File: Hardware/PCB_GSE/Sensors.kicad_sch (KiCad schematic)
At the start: 19 parts, among them J18 Screw_Terminal_01x04, J19 Screw_Terminal_01x04, U4 INA125UA/2K5, U6 INA125UA/2K5, U9 MAX6612MXK

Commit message: refactor: merge emile + main branches
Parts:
- renumbered C45 to C48, C44 to C49, C49 to C50, C48 to C51, C46 to C52, C47 to C53, J18 to J7, J19 to J8, R55 to R33, R53 to R34, R56 to R35, R54 to R36, R58 to R37, R57 to R38, U4 to U10, U9 to U11, U6 to U9

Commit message: fix: labels
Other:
- moved on the sheet: C48, C51, D6, J7, R33, R35, R38, U9

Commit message: wip : Reduce BOM and fill all datasheet, digikey and MPN
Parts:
- C48, C49, C50, C51, C53: footprint Capacitor_SMD:C_0805_2012Metric -> Capacitor_SMD:C_0603_1608Metric; DigiKey_Part_Number (none) -> 399-C0603C104K3RACTUCT-ND; Manufacturer_Part_Number (none) -> C0603C104K3RACTU
- C52: footprint Capacitor_SMD:C_0603_1608Metric -> Capacitor_SMD:C_0805_2012Metric; DigiKey_Part_Number (none) -> 1276-2434-1-ND; Manufacturer_Part_Number (none) -> CL21B103KAANNNC
- D5, D6: DigiKey_Part_Number (none) -> 4878-BAT54SCT-ND; Manufacturer_Part_Number (none) -> BAT54S
- J7, J8: DigiKey_Part_Number (none) -> ED10563-ND; Manufacturer_Part_Number (none) -> OSTVN04A150
- R33, R34: DigiKey_Part_Number (none) -> 311-10.0KHRCT-ND; Manufacturer_Part_Number (none) -> RC0603FR-0710KL
- R35: DigiKey_Part_Number (none) -> YAG3707CT-ND; Manufacturer_Part_Number (none) -> AC0805FR-07200RL
- R36: DigiKey_Part_Number (none) -> 311-1.00KCRCT-ND; Manufacturer_Part_Number (none) -> RC0805FR-071KL
- R37, R38: DigiKey_Part_Number (none) -> P1.5KDBCT-ND; Manufacturer_Part_Number (none) -> ERA-3AEB152V
- U10, U9: DigiKey_Part_Number (none) -> 296-50343-1-ND; DigiKey_Part_Number  296-50343-1-ND -> (none)

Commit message: wip: begining layout
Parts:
- renumbered R33 to R36, R34 to R37, R35 to R38, R36 to R39, R37 to R40, R38 to R41

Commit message: wip : subsystems layout
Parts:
- renumbered C48 to C57, C49 to C58, C50 to C59, C51 to C60, C52 to C61, C53 to C62, D5 to D4, D6 to D5, R36 to R44, R37 to R45, R38 to R46, R39 to R47, R40 to R48, R41 to R49

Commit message: wip : Done routing
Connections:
- net +3.3VA is gone; now on net +3V3: D4.2 (K), D5.2 (K)
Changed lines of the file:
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@@
-	)
-	(symbol
-		(lib_id "power:+3.3VA")
-		(at 127 130.81 0)
-		(unit 1)
-		(exclude_from_sim no)
-		(in_bom yes)
-		(on_board yes)
-		(dnp no)
-		(property "Reference" "#PWR0222"
-			(at 127 134.62 0)
-			(effects
-				(font
-					(size 1 1)
-				)
-				(hide yes)
-			)
-		)
-		(property "Value" "+3.3VA"
-			(at 127 127 0)
-			(effects
-				(font
-					(size 1 1)
-				)
-			)
-		)
-		(property "Footprint" ""
-			(at 127 130.81 0)
-			(effects
-				(font
-					(size 1 1)
-				)
-				(hide yes)
-			)
-		)
-		(property "Datasheet" ""
-			(at 127 130.81 0)
-			(effects
-				(font
-					(size 1 1)
-				)
-				(hide yes)
-			)
-		)
-		(property "Description" ""
-			(at 127 130.81 0)
-			(effects
-				(font
-					(size 1.27 1.27)
-				)
-			)
-		)
-		(pin "1"
-		)
-		(instances
-			(project "PCB_GSE"
-				(path "/a63f9ed4-21e4-42d0-8bfc-f96143f84d4d/03aa44f0-76dc-422b-9f36-66afc2e68b3b"
-					(reference "#PWR0222")
-					(unit 1)
-				)
-			)
-		)
 	)
 	(symbol
@@
 	)
 	(symbol
+		(lib_id "power:+3V3")
+		(at 127 130.81 0)
+		(unit 1)
+		(exclude_from_sim no)
+		(in_bom yes)
+		(on_board yes)
+		(dnp no)
+		(property "Reference" "#PWR03"
+			(at 127 134.62 0)
+			(effects
+				(font
+					(size 1.27 1.27)
+				)
+				(hide yes)
+			)
+		)
+		(property "Value" "+3V3"
+			(at 127 127 0)
+			(effects
+				(font
+					(size 1.27 1.27)
+				)
+			)
+		)
+		(property "Footprint" ""
+			(at 127 130.81 0)
+			(effects
+				(font
+					(size 1.27 1.27)
+				)
+				(hide yes)
+			)
+		)
+		(property "Datasheet" ""
+			(at 127 130.81 0)
+			(effects
+				(font
+					(size 1.27 1.27)
+				)
+				(hide yes)
+			)
+		)
+		(property "Description" "Power symbol creates a global label with name \"+3V3\""
+			(at 127 130.81 0)
+			(effects
+				(font
+					(size 1.27 1.27)
+				)
+				(hide yes)
+			)
+		)
+		(pin "1"
+		)
+		(instances
+			(project "PCB_GSE"
+				(path "/a63f9ed4-21e4-42d0-8bfc-f96143f84d4d/03aa44f0-76dc-422b-9f36-66afc2e68b3b"
+					(reference "#PWR03")
+					(unit 1)
+				)
+			)
+		)
+	)
+	(symbol
 		(lib_id "Device:C")
 		(at 257.81 44.45 0)
@@
 	)
 	(symbol
+		(lib_id "power:+3V3")
+		(at 127 57.15 0)
+		(unit 1)
+		(exclude_from_sim no)
+		(in_bom yes)
+		(on_board yes)
+		(dnp no)
+		(property "Reference" "#PWR04"
+			(at 127 60.96 0)
+			(effects
+				(font
+					(size 1.27 1.27)
+				)
+				(hide yes)
+			)
+		)
+		(property "Value" "+3V3"
+			(at 127 53.34 0)
+			(effects
+				(font
+					(size 1.27 1.27)
+				)
+			)
+		)
+		(property "Footprint" ""
+			(at 127 57.15 0)
+			(effects
+				(font
+					(size 1.27 1.27)
+				)
+				(hide yes)
+			)
+		)
+		(property "Datasheet" ""
+			(at 127 57.15 0)
+			(effects
+				(font
+					(size 1.27 1.27)
+				)
+				(hide yes)
+			)
+		)
+		(property "Description" "Power symbol creates a global label with name \"+3V3\""
+			(at 127 57.15 0)
+			(effects
+				(font
+					(size 1.27 1.27)
+				)
+				(hide yes)
+			)
+		)
+		(pin "1"
+		)
+		(instances
+			(project "PCB_GSE"
+				(path "/a63f9ed4-21e4-42d0-8bfc-f96143f84d4d/03aa44f0-76dc-422b-9f36-66afc2e68b3b"
+					(reference "#PWR04")
+					(unit 1)
+				)
+			)
+		)
+	)
+	(symbol
 		(lib_id "power:GND")
 		(at 220.98 50.8 0)
@@
 					(unit 1)
 				)
-			)
-		)
-	)
-	(symbol
-		(lib_id "power:+3.3VA")
-		(at 127 57.15 0)
-		(unit 1)
-		(exclude_from_sim no)
-		(in_bom yes)
-		(on_board yes)
-		(dnp no)
-		(property "Reference" "#PWR0217"
-			(at 127 60.96 0)
-			(effects
-				(font
-					(size 1 1)
-				)
-				(hide yes)
-			)
-		)
-		(property "Value" "+3.3VA"
-			(at 127 53.34 0)
-			(effects
-				(font
-					(size 1 1)
-				)
-			)
-		)
-		(property "Footprint" ""
-			(at 127 57.15 0)
-			(effects
-				(font
-					(size 1 1)
-				)
-				(hide yes)
-			)
-		)
-		(property "Datasheet" ""
-			(at 127 57.15 0)
-			(effects
-				(font
-					(size 1 1)
-				)
-				(hide yes)
-			)
-		)
-		(property "Description" ""
-			(at 127 57.15 0)
-			(effects
-				(font
-					(size 1.27 1.27)
-				)
-			)
-		)
-		(pin "1"
-		)
-		(instances
-			(project "PCB_GSE"
-				(path "/a63f9ed4-21e4-42d0-8bfc-f96143f84d4d/03aa44f0-76dc-422b-9f36-66afc2e68b3b"
-					(reference "#PWR0217")
-					(unit 1)
-				)

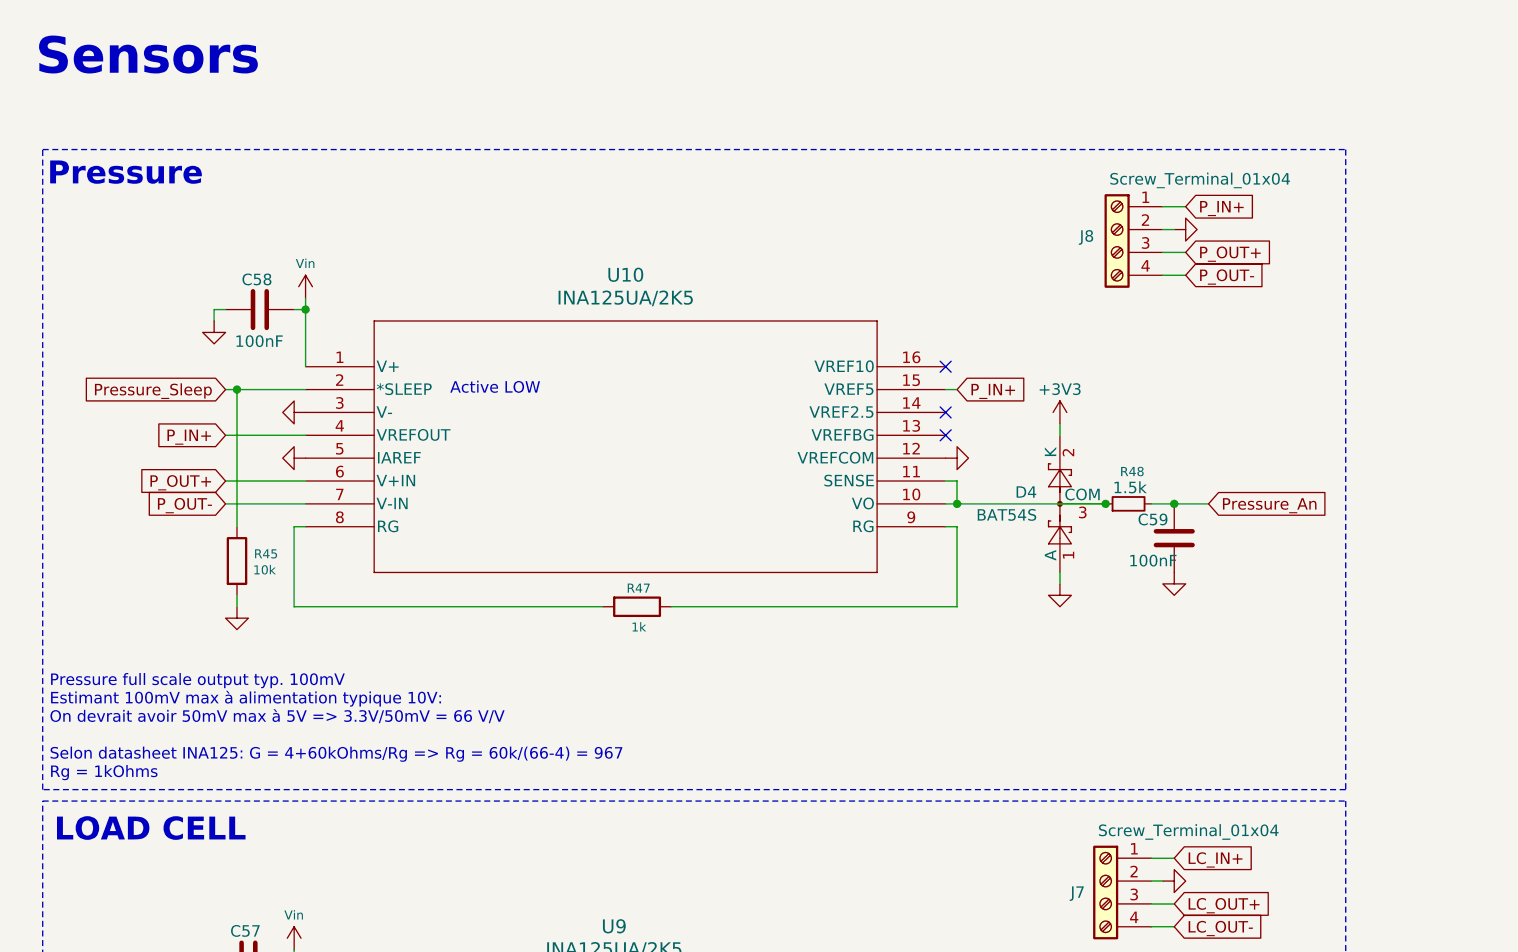
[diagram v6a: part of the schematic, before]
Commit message: fix : replace Pressure sensor amplification circuit with new voltage divider circuit
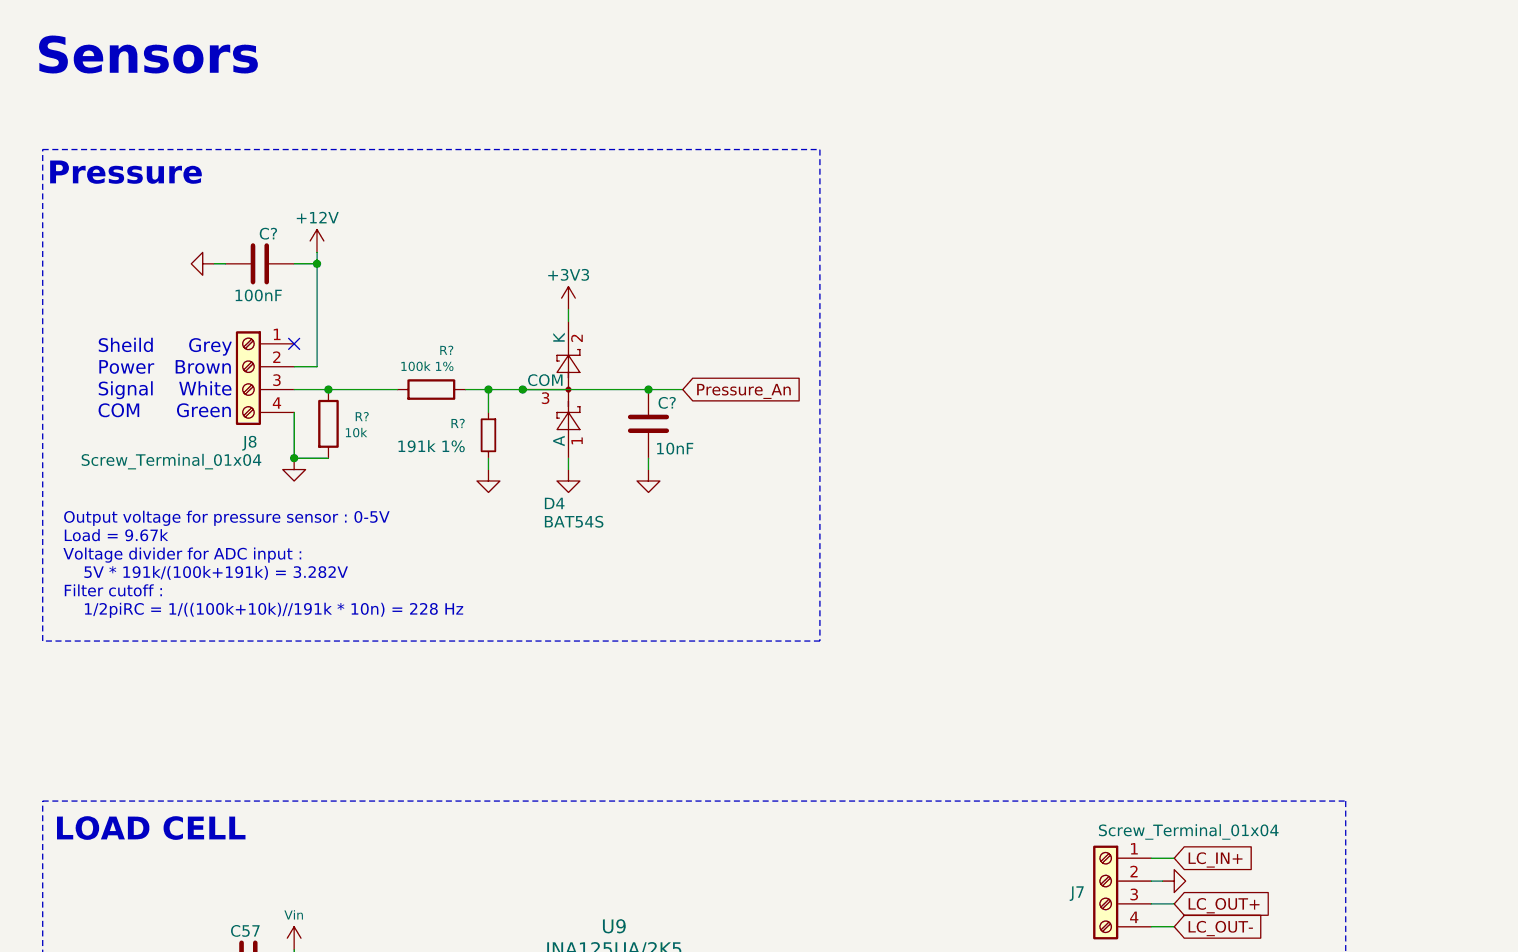
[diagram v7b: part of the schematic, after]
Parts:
- removed C58, C59: 100nF, Capacitor_SMD:C_0603_1608Metric, symbol Device:C
- removed R45: 10k, Resistor_SMD:R_0805_2012Metric, symbol Device:R
- removed R47: 1k, Resistor_SMD:R_0805_2012Metric, symbol Device:R
- removed R48: 1.5k, Resistor_SMD:R_0805_2012Metric, symbol Device:R_Small
- removed U10: INA125UA/2K5, pcb_moteur:D16-L, symbol PCB_GSE:INA125UA_2K5
- added C?: 100nF, Capacitor_SMD:C_0603_1608Metric, symbol Device:C
- added C?: 10nF, Capacitor_SMD:C_0805_2012Metric, symbol Device:C
- added R?: 191k 1%, Resistor_SMD:R_0805_2012Metric, symbol Device:R_Small
- added R?: 10k, Resistor_SMD:R_0805_2012Metric, symbol Device:R
- added R?: 100k 1%, Resistor_SMD:R_0805_2012Metric, symbol Device:R
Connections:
- net P_OUT- is gone; now on net GND: J8.4 (Pin_4)
- net GND: now also C?.1, C?.2, R?.2, R?.2; no longer J8.2 (Pin_2)
- net Pressure_An: now also D4.3 (COM), C?.1, R?.1, R?.1
- net P_IN+: no longer names the net of J8.1 (Pin_1)
- net P_OUT+: no longer names the net of J8.3 (Pin_3)
- net P_OUT+: now also R?.1, R?.2
- new net +12V: C?.2, J8.2 (Pin_2)
- no-connect marks 6 -> 4
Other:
- note added: "Grey Brown White Green"
- note added: "Output voltage for pressure sensor : 0-5V Load = 9.67k Voltage divider for ADC input : 5V * 191k/(100k+191k) = 3.282V Filter cutoff : 1/2piRC = 1/((100k+10k)//191k * 10n) = 228 Hz"
- note added: "Sheild Power Signal COM"
- note removed: "Pressure full scale output typ. 100mV Estimant 100mV max à alimentation typique 10V: On devrait avoir 50mV max à 5V => 3.3V/50mV = 66 V/V Selon datasheet INA125: G = 4+60kOhms/Rg => Rg = 60k/(66-4) = 967 Rg = 1kOhms"
- moved on the sheet: D4, J8

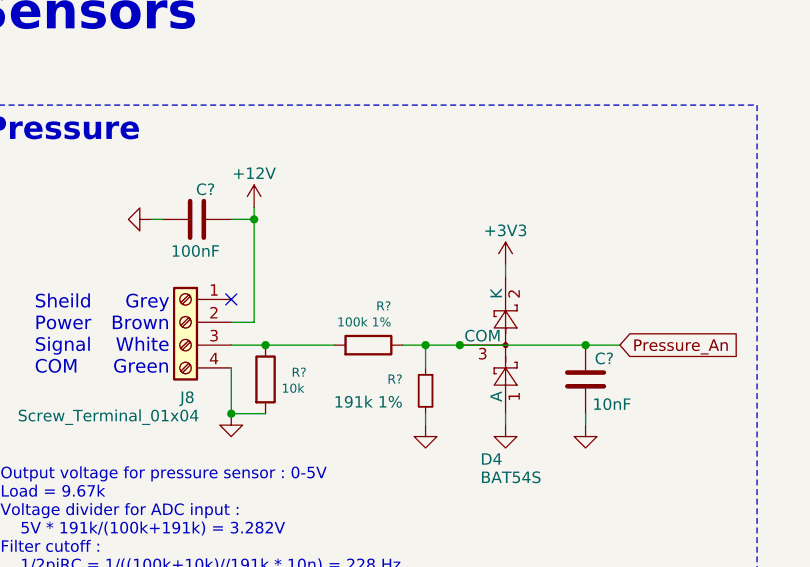
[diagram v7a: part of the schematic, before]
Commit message: fix : routing des modifications Servo et capteur pression
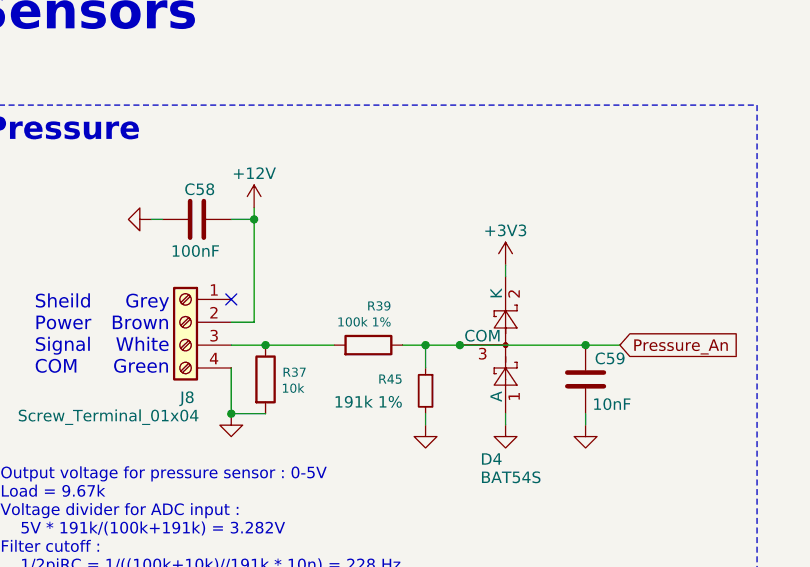
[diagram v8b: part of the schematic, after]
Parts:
- gave numbers to parts that had none: 5
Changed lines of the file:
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@@
 		(on_board yes)
 		(dnp no)
-		(property "Reference" "R?"
+		(property "Reference" "R45"
 			(at 60.96 57.1499 0)
 			(effects
@@
 			(project "PCB_GSE"
 				(path "/a63f9ed4-21e4-42d0-8bfc-f96143f84d4d/03aa44f0-76dc-422b-9f36-66afc2e68b3b"
-					(reference "R?")
+					(reference "R45")
 					(unit 1)
 				)
@@
 		(on_board yes)
 		(dnp no)
-		(property "Reference" "R?"
+		(property "Reference" "R37"
 			(at 50.292 56.388 0)
 			(effects
@@
 			(project "PCB_GSE"
 				(path "/a63f9ed4-21e4-42d0-8bfc-f96143f84d4d/03aa44f0-76dc-422b-9f36-66afc2e68b3b"
-					(reference "R?")
+					(reference "R37")
 					(unit 1)
 				)
@@
 		(on_board yes)
 		(dnp no)
-		(property "Reference" "R?"
+		(property "Reference" "R39"
 			(at 59.69 49.022 90)
 			(effects
@@
 			(project "PCB_GSE"
 				(path "/a63f9ed4-21e4-42d0-8bfc-f96143f84d4d/03aa44f0-76dc-422b-9f36-66afc2e68b3b"
-					(reference "R?")
+					(reference "R39")
 					(unit 1)
 				)
@@
 		(on_board yes)
 		(dnp no)
-		(property "Reference" "C?"
+		(property "Reference" "C58"
 			(at 40.132 36.068 90)
 			(effects
@@
 			(project "PCB_GSE"
 				(path "/a63f9ed4-21e4-42d0-8bfc-f96143f84d4d/03aa44f0-76dc-422b-9f36-66afc2e68b3b"
-					(reference "C?")
+					(reference "C58")
 					(unit 1)
 				)
@@
 		(on_board yes)
 		(dnp no)
-		(property "Reference" "C?"
+		(property "Reference" "C59"
 			(at 82.296 54.864 0)
 			(effects
@@
 			(project "PCB_GSE"
 				(path "/a63f9ed4-21e4-42d0-8bfc-f96143f84d4d/03aa44f0-76dc-422b-9f36-66afc2e68b3b"
-					(reference "C?")
-					(unit 1)
-				)
+					(reference "C59")
+					(unit 1)
+				)
